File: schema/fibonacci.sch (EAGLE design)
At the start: 29 parts, among them IC1 DS1307, J1 POWER_JACK

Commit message: Board schema and layout v0.9
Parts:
- removed C6: 100nF, resistor:C-EU050-025X075
- removed U$1: RPI_SD_HOLDER, xose:RPI_SD_HOLDER
- added C3: 100nF, xose:C-EU050-025X075
- added U$2: MicroSD, xose:MICROSD-HRS_DM3D
- 16MHZ: value (none) -> 16MHz; device special:XTAL/S -> xose:XTAL/S
- BATT: device adafruit:CR2032SMT -> xose:CR2032SMT
- BUTTON1: value TACTILE_BUTTON -> B1
- BUTTON2: value TACTILE_BUTTON -> B2
- BUTTON3: value TACTILE_BUTTON -> B3
- BUTTON4: value TACTILE_BUTTON -> B4
- C1, C2, C4, C5: device rcl:C-EU025-025X050 -> xose:C-EU050-025X075
- CRYSTAL: device adafruit:CRYSTALTC38H -> xose:CRYSTAL_TC38H
- IC1: device adafruit:DS1307 -> xose:DS1307
- J1: value POWER_JACK -> POWER_JACKPTH; device SparkFun-Connectors:POWER_JACKPTH -> xose:POWER_JACKPTH
- LED_TERMINAL: value (none) -> M03-SCREW-2.5MM; device SparkFun-Connectors:M03-SCREW-5MM -> xose:M03-SCREW-2.5MM
- MUC: device SparkFun-DigitalIC:ATMEGA328P_PDIP -> xose:ATMEGA328P_PDIP
- POWER_TERMINAL: value (none) -> M02-SCREW-2.5MM; device SparkFun-Connectors:M025MM -> xose:M02-SCREW-2.5MM
- R1, R2, R3, R4, R5, R6, R7, R8: device SparkFun-Resistors:RESISTORPTH-1/4W -> xose:RESISTOR
- R9: value 10K -> 1K8; device SparkFun-Resistors:RESISTORPTH-1/4W -> xose:RESISTOR
- REGULATOR: value LP2950Z -> TSC295033; device national-semiconductor:LP2950Z -> xose:LP2950Z
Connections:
- new net N$14: U$2.GND1
- new net N$15: U$2.GND2
- new net N$16: U$2.GND3
- new net N$17: U$2.GND4
- net 3V3: now also U$2.3V3; no longer U$1.3V3
- net 5V: now also POWER_TERMINAL.1, R9.2; no longer POWER_TERMINAL.2, R9.1
- net DATA: now also MUC.PD4(XCK/T0); no longer MUC.PB1(OC1A)
- net DTR: now also C3.2; no longer C6.1
- net GND: now also C4.2, C5.2, POWER_TERMINAL.2, U$2.CMD, U$2.VSS; no longer C4.1, C5.1, POWER_TERMINAL.1, U$1.GND1, U$1.GND2
- net MISO: now also U$2.MISO; no longer U$1.MISO
- net N$1: now also C3.1, R9.1; no longer C6.2, R9.2
- net N$2: now also C4.1; no longer C4.2
- net N$3: now also C5.1; no longer C5.2
- net N$4: now also BATT.+; no longer BATT.+1
- net SD_MOSI: now also U$2.MOSI; no longer U$1.MOSI
- net SD_SCK: now also U$2.SCK; no longer U$1.SCK
- net SD_SS: now also U$2.SS; no longer U$1.SS
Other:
- moved on the sheet: BATT, C4, C5, POWER_TERMINAL

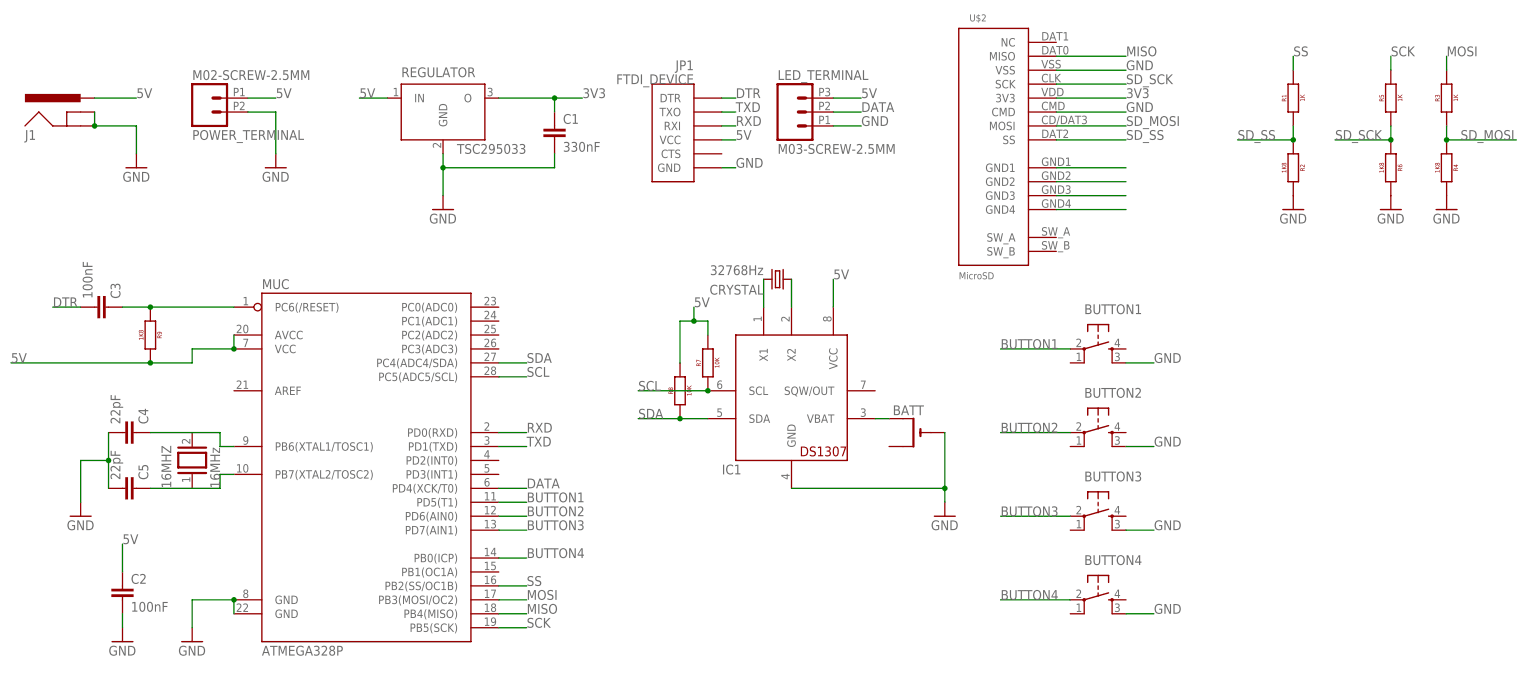
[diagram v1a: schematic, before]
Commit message: Added beefier terminals to board
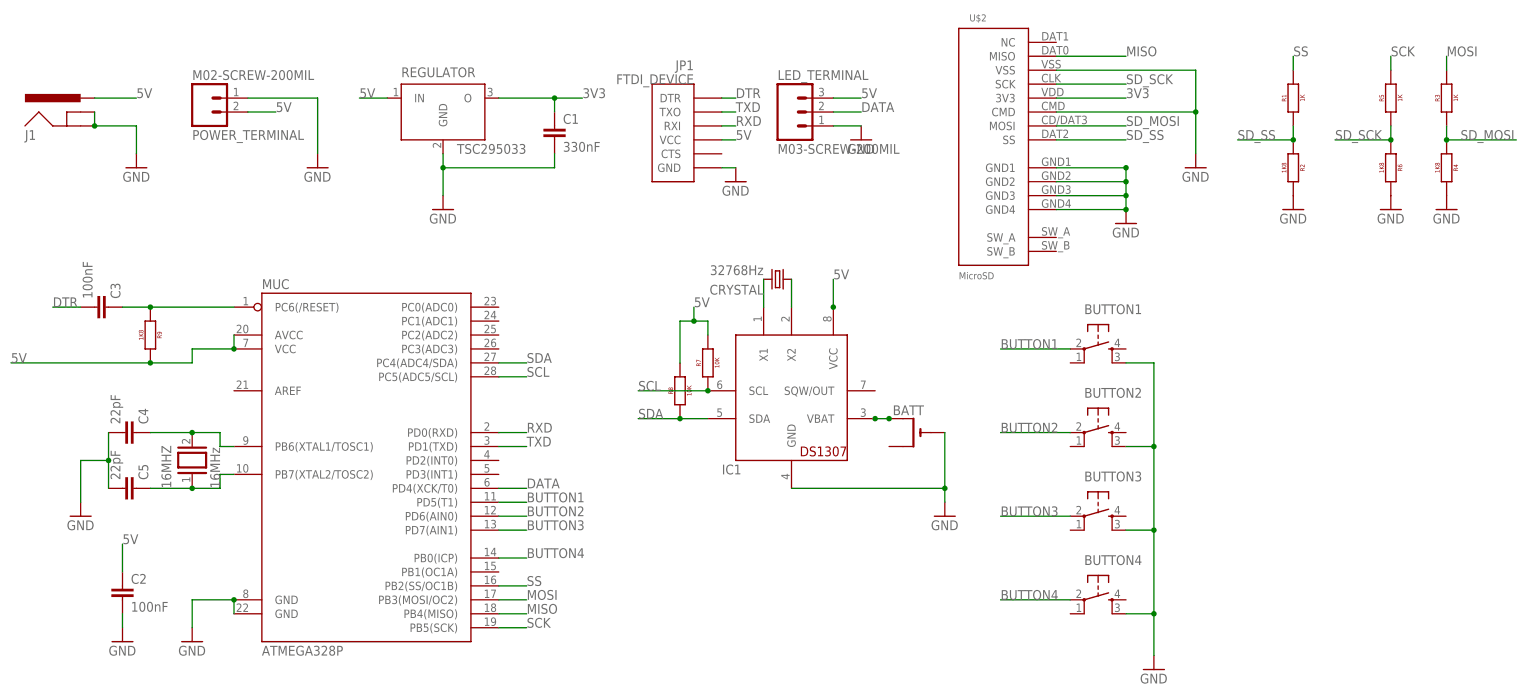
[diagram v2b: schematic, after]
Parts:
- LED_TERMINAL: value M03-SCREW-2.5MM -> M03-SCREW-200MIL; device xose:M03-SCREW-2.5MM -> xose:M03-SCREW-200MIL
- POWER_TERMINAL: value M02-SCREW-2.5MM -> M02-SCREW-200MIL; device xose:M02-SCREW-2.5MM -> xose:M02-SCREW-200MIL
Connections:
- removed net N$14: U$2.GND1
- removed net N$15: U$2.GND2
- removed net N$16: U$2.GND3
- removed net N$17: U$2.GND4
- net 5V: now also POWER_TERMINAL.2; no longer POWER_TERMINAL.1
- net GND: now also POWER_TERMINAL.1, U$2.GND1, U$2.GND2, U$2.GND3, U$2.GND4; no longer POWER_TERMINAL.2
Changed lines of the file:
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@@
 <part name="BUTTON3" library="xose" deviceset="TACTILE_BUTTON" device="" value="B3"/>
 <part name="BUTTON4" library="xose" deviceset="TACTILE_BUTTON" device="" value="B4"/>
-<part name="POWER_TERMINAL" library="xose" deviceset="M02-SCREW-2.5MM" device=""/>
-<part name="LED_TERMINAL" library="xose" deviceset="M03-SCREW-2.5MM" device=""/>
+<part name="POWER_TERMINAL" library="xose" deviceset="M02-SCREW-200MIL" device=""/>
+<part name="LED_TERMINAL" library="xose" deviceset="M03-SCREW-200MIL" device=""/>
 <part name="GND1" library="SparkFun-Aesthetics" deviceset="GND" device=""/>
 <part name="GND5" library="SparkFun-Aesthetics" deviceset="GND" device=""/>
@@
 <part name="R9" library="xose" deviceset="RESISTOR" device="" value="1K8"/>
 <part name="U$2" library="xose" deviceset="MICROSD-HRS_DM3D" device="" value="MicroSD"/>
+<part name="GND11" library="SparkFun-Aesthetics" deviceset="GND" device=""/>
+<part name="GND12" library="SparkFun-Aesthetics" deviceset="GND" device=""/>
+<part name="GND13" library="SparkFun-Aesthetics" deviceset="GND" device=""/>
+<part name="GND14" library="SparkFun-Aesthetics" deviceset="GND" device=""/>
+<part name="GND15" library="SparkFun-Aesthetics" deviceset="GND" device=""/>
 </parts>
 <sheets>
@@
 <instance part="POWER_TERMINAL" gate="G$1" x="-10.16" y="96.52" rot="MR180"/>
 <instance part="LED_TERMINAL" gate="G$1" x="96.52" y="96.52"/>
-<instance part="GND1" gate="1" x="2.54" y="86.36"/>
+<instance part="GND1" gate="1" x="10.16" y="86.36"/>
 <instance part="GND5" gate="1" x="124.46" y="22.86"/>
 <instance part="GND7" gate="1" x="33.02" y="78.74"/>
@@
 <instance part="R9" gate="G$1" x="-20.32" y="55.88" rot="R270"/>
 <instance part="U$2" gate="G$1" x="127" y="86.36"/>
+<instance part="GND11" gate="1" x="157.48" y="76.2"/>
+<instance part="GND12" gate="1" x="170.18" y="86.36"/>
+<instance part="GND13" gate="1" x="109.22" y="91.44"/>
+<instance part="GND14" gate="1" x="86.36" y="83.82"/>
+<instance part="GND15" gate="1" x="162.56" y="-5.08"/>
 </instances>
 <busses>
@@
 </segment>
 <segment>
-<pinref part="GND1" gate="1" pin="GND"/>
-<wire x1="2.54" y1="96.52" x2="2.54" y2="88.9" width="0.1524" layer="91"/>
-<pinref part="POWER_TERMINAL" gate="G$1" pin="2"/>
-<wire x1="2.54" y1="96.52" x2="-2.54" y2="96.52" width="0.1524" layer="91"/>
-</segment>
-<segment>
 <pinref part="LED_TERMINAL" gate="G$1" pin="1"/>
 <wire x1="104.14" y1="93.98" x2="109.22" y2="93.98" width="0.1524" layer="91"/>
-<label x="109.22" y="93.98" size="1.778" layer="95"/>
+<pinref part="GND13" gate="1" pin="GND"/>
 </segment>
 <segment>
@@
 <pinref part="BUTTON1" gate="G$1" pin="SWB2"/>
 <wire x1="157.48" y1="50.8" x2="162.56" y2="50.8" width="0.1524" layer="91"/>
-<label x="162.56" y="50.8" size="1.778" layer="95"/>
-</segment>
-<segment>
+<pinref part="GND15" gate="1" pin="GND"/>
+<wire x1="162.56" y1="50.8" x2="162.56" y2="35.56" width="0.1524" layer="91"/>
+<pinref part="BUTTON4" gate="G$1" pin="SWB2"/>
+<wire x1="162.56" y1="35.56" x2="162.56" y2="20.32" width="0.1524" layer="91"/>
+<wire x1="162.56" y1="20.32" x2="162.56" y2="5.08" width="0.1524" layer="91"/>
+<wire x1="162.56" y1="5.08" x2="162.56" y2="-2.54" width="0.1524" layer="91"/>
+<wire x1="157.48" y1="5.08" x2="162.56" y2="5.08" width="0.1524" layer="91"/>
+<junction x="162.56" y="5.08"/>
+<pinref part="BUTTON3" gate="G$1" pin="SWB2"/>
+<wire x1="157.48" y1="20.32" x2="162.56" y2="20.32" width="0.1524" layer="91"/>
+<junction x="162.56" y="20.32"/>
 <pinref part="BUTTON2" gate="G$1" pin="SWB2"/>
 <wire x1="157.48" y1="35.56" x2="162.56" y2="35.56" width="0.1524" layer="91"/>
-<label x="162.56" y="35.56" size="1.778" layer="95"/>
-</segment>
-<segment>
-<pinref part="BUTTON3" gate="G$1" pin="SWB2"/>
-<wire x1="157.48" y1="20.32" x2="162.56" y2="20.32" width="0.1524" layer="91"/>
-<label x="162.56" y="20.32" size="1.778" layer="95"/>
-</segment>
-<segment>
-<pinref part="BUTTON4" gate="G$1" pin="SWB2"/>
-<wire x1="157.48" y1="5.08" x2="162.56" y2="5.08" width="0.1524" layer="91"/>
-<label x="162.56" y="5.08" size="1.778" layer="95"/>
+<junction x="162.56" y="35.56"/>
 </segment>
 <segment>
 <pinref part="JP1" gate="G$1" pin="GND"/>
 <wire x1="83.82" y1="86.36" x2="86.36" y2="86.36" width="0.1524" layer="91"/>
-<label x="86.36" y="86.36" size="1.778" layer="95"/>
+<pinref part="GND14" gate="1" pin="GND"/>
 </segment>
 <segment>
 <pinref part="U$2" gate="G$1" pin="VSS"/>
-<wire x1="144.78" y1="104.14" x2="157.48" y2="104.14" width="0.1524" layer="91"/>
-<label x="157.48" y="104.14" size="1.778" layer="95"/>
-</segment>
-<segment>
-<wire x1="144.78" y1="96.52" x2="157.48" y2="96.52" width="0.1524" layer="91"/>
-<label x="157.48" y="96.52" size="1.778" layer="95"/>
+<wire x1="144.78" y1="104.14" x2="170.18" y2="104.14" width="0.1524" layer="91"/>
+<wire x1="170.18" y1="104.14" x2="170.18" y2="96.52" width="0.1524" layer="91"/>
 <pinref part="U$2" gate="G$1" pin="CMD"/>
+<wire x1="170.18" y1="96.52" x2="170.18" y2="88.9" width="0.1524" layer="91"/>
+<wire x1="144.78" y1="96.52" x2="170.18" y2="96.52" width="0.1524" layer="91"/>
+<pinref part="GND12" gate="1" pin="GND"/>
+<junction x="170.18" y="96.52"/>
+</segment>
+<segment>
+<pinref part="U$2" gate="G$1" pin="GND4"/>
+<wire x1="144.78" y1="78.74" x2="157.48" y2="78.74" width="0.1524" layer="91"/>
+<pinref part="GND11" gate="1" pin="GND"/>
+<pinref part="U$2" gate="G$1" pin="GND1"/>
+<wire x1="144.78" y1="86.36" x2="157.48" y2="86.36" width="0.1524" layer="91"/>
+<wire x1="157.48" y1="86.36" x2="157.48" y2="83.82" width="0.1524" layer="91"/>
+<pinref part="U$2" gate="G$1" pin="GND3"/>
+<wire x1="157.48" y1="83.82" x2="157.48" y2="81.28" width="0.1524" layer="91"/>
+<wire x1="157.48" y1="81.28" x2="157.48" y2="78.74" width="0.1524" layer="91"/>
+<wire x1="144.78" y1="81.28" x2="157.48" y2="81.28" width="0.1524" layer="91"/>
+<junction x="157.48" y="81.28"/>
+<pinref part="U$2" gate="G$1" pin="GND2"/>
+<wire x1="144.78" y1="83.82" x2="157.48" y2="83.82" width="0.1524" layer="91"/>
+<junction x="157.48" y="83.82"/>
+<junction x="157.48" y="78.74"/>
+<junction x="157.48" y="86.36"/>
+</segment>
+<segment>
+<pinref part="POWER_TERMINAL" gate="G$1" pin="1"/>
+<wire x1="-2.54" y1="99.06" x2="10.16" y2="99.06" width="0.1524" layer="91"/>
+<wire x1="10.16" y1="99.06" x2="10.16" y2="88.9" width="0.1524" layer="91"/>
+<pinref part="GND1" gate="1" pin="GND"/>
 </segment>
 </net>
@@
 <wire x1="104.14" y1="60.96" x2="104.14" y2="66.04" width="0.1524" layer="91"/>
 <label x="104.14" y="66.04" size="1.778" layer="95"/>
+<junction x="104.14" y="60.96"/>
 </segment>
 <segment>
@@
 </segment>
 <segment>
-<pinref part="POWER_TERMINAL" gate="G$1" pin="1"/>
-<wire x1="-2.54" y1="99.06" x2="2.54" y2="99.06" width="0.1524" layer="91"/>
-<label x="2.54" y="99.06" size="1.778" layer="95"/>
+<pinref part="POWER_TERMINAL" gate="G$1" pin="2"/>
+<wire x1="-2.54" y1="96.52" x2="2.54" y2="96.52" width="0.1524" layer="91"/>
+<label x="2.54" y="96.52" size="1.778" layer="95"/>
 </segment>
 </net>
@@
 <pinref part="C4" gate="G$1" pin="1"/>
 <wire x1="-12.7" y1="38.1" x2="-20.32" y2="38.1" width="0.1524" layer="91"/>
+<junction x="-12.7" y="38.1"/>
 </segment>
 </net>
@@
 <pinref part="C5" gate="G$1" pin="1"/>
 <wire x1="-12.7" y1="27.94" x2="-20.32" y2="27.94" width="0.1524" layer="91"/>
+<junction x="-12.7" y="27.94"/>
 </segment>
 </net>
@@
 </segment>
 </net>
-<net name="N$14" class="0">
-<segment>
-<pinref part="U$2" gate="G$1" pin="GND1"/>
-<wire x1="144.78" y1="86.36" x2="157.48" y2="86.36" width="0.1524" layer="91"/>
-</segment>
-</net>
-<net name="N$15" class="0">
-<segment>
-<pinref part="U$2" gate="G$1" pin="GND2"/>
-<wire x1="144.78" y1="83.82" x2="157.48" y2="83.82" width="0.1524" layer="91"/>
-</segment>
-</net>
-<net name="N$16" class="0">
-<segment>
-<pinref part="U$2" gate="G$1" pin="GND3"/>
-<wire x1="144.78" y1="81.28" x2="157.48" y2="81.28" width="0.1524" layer="91"/>
-</segment>
-</net>
-<net name="N$17" class="0">
-<segment>
-<pinref part="U$2" gate="G$1" pin="GND4"/>
-<wire x1="144.78" y1="78.74" x2="157.48" y2="78.74" width="0.1524" layer="91"/>
-</segment>
-</net>
 <net name="N$4" class="0">
 <segment>
@@
 <pinref part="BATT" gate="G$1" pin="+"/>
 <wire x1="111.76" y1="40.64" x2="114.3" y2="40.64" width="0.1524" layer="91"/>
-</segment>
-</net>
+<junction x="114.3" y="40.64"/>
+<junction x="111.76" y="40.64"/>
+</segment>
+</net>

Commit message: Final PCB version and gerbers
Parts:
- removed MUC: ATMEGA328P, xose:ATMEGA328P_PDIP
- added IC2: DS1307, xose:DS1307
- IC1: value DS1307 -> ATMEGA328P; device xose:DS1307 -> xose:ATMEGA328P_PDIP
- U$2: value MicroSD -> uSD
- renumbered 16MHZ to XTAL1, CRYSTAL to XTAL2, REGULATOR to LDO1
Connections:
- net 5V: now also IC1.AVCC, IC2.VCC; no longer MUC.AVCC, MUC.VCC
- net BUTTON1: now also IC1.PD5(T1); no longer MUC.PD5(T1)
- net BUTTON2: now also IC1.PD6(AIN0); no longer MUC.PD6(AIN0)
- net BUTTON3: now also IC1.PD7(AIN1); no longer MUC.PD7(AIN1)
- net BUTTON4: now also IC1.PB0(ICP); no longer MUC.PB0(ICP)
- net DATA: now also IC1.PD4(XCK/T0); no longer MUC.PD4(XCK/T0)
- net GND: now also IC1.GND@1, IC1.GND@2, IC2.GND; no longer IC1.GND, MUC.GND@1, MUC.GND@2
- net MISO: now also IC1.PB4(MISO); no longer MUC.PB4(MISO)
- net MOSI: now also IC1.PB3(MOSI/OC2); no longer MUC.PB3(MOSI/OC2)
- net N$1: now also IC1.PC6(/RESET); no longer MUC.PC6(/RESET)
- net N$2: now also IC1.PB6(XTAL1/TOSC1); no longer MUC.PB6(XTAL1/TOSC1)
- net N$3: now also IC1.PB7(XTAL2/TOSC2); no longer MUC.PB7(XTAL2/TOSC2)
- net N$4: now also IC2.VBAT; no longer IC1.VBAT
- net N$5: now also IC2.X1; no longer IC1.X1
- net N$6: now also IC2.X2; no longer IC1.X2
- net RXD: now also IC1.PD0(RXD); no longer MUC.PD0(RXD)
- net SCK: now also IC1.PB5(SCK); no longer MUC.PB5(SCK)
- net SCL: now also IC1.PC5(ADC5/SCL), IC2.SCL; no longer IC1.SCL, MUC.PC5(ADC5/SCL)
- net SDA: now also IC1.PC4(ADC4/SDA), IC2.SDA; no longer IC1.SDA, MUC.PC4(ADC4/SDA)
- net SS: now also IC1.PB2(SS/OC1B); no longer MUC.PB2(SS/OC1B)
- net TXD: now also IC1.PD1(TXD); no longer MUC.PD1(TXD)

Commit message: Schema and board layout, datasheets
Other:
- moved on the sheet: LDO1

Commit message: Version 1.2 of the layout sent to fab
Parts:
- R1, R2, R3, R4, R5, R6, R7, R8, R9: device xose:RESISTOR -> xose:RESISTOR-400MIL
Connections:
- net GND: no longer U$2.CMD
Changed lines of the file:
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@@
 <part name="IC2" library="xose" deviceset="DS1307" device=""/>
 <part name="XTAL2" library="xose" deviceset="CRYSTAL_TC38H" device="" value="32768Hz"/>
-<part name="R1" library="xose" deviceset="RESISTOR" device="" value="1K"/>
-<part name="R3" library="xose" deviceset="RESISTOR" device="" value="1K"/>
-<part name="R5" library="xose" deviceset="RESISTOR" device="" value="1K"/>
-<part name="R2" library="xose" deviceset="RESISTOR" device="" value="1K8"/>
-<part name="R4" library="xose" deviceset="RESISTOR" device="" value="1K8"/>
-<part name="R6" library="xose" deviceset="RESISTOR" device="" value="1K8"/>
-<part name="R7" library="xose" deviceset="RESISTOR" device="" value="10K"/>
-<part name="R8" library="xose" deviceset="RESISTOR" device="" value="10K"/>
+<part name="R1" library="xose" deviceset="RESISTOR-400MIL" device="" value="1K"/>
+<part name="R3" library="xose" deviceset="RESISTOR-400MIL" device="" value="1K"/>
+<part name="R5" library="xose" deviceset="RESISTOR-400MIL" device="" value="1K"/>
+<part name="R2" library="xose" deviceset="RESISTOR-400MIL" device="" value="1K8"/>
+<part name="R4" library="xose" deviceset="RESISTOR-400MIL" device="" value="1K8"/>
+<part name="R6" library="xose" deviceset="RESISTOR-400MIL" device="" value="1K8"/>
+<part name="R7" library="xose" deviceset="RESISTOR-400MIL" device="" value="10K"/>
+<part name="R8" library="xose" deviceset="RESISTOR-400MIL" device="" value="10K"/>
 <part name="BUTTON1" library="xose" deviceset="TACTILE_BUTTON" device="" value="B1"/>
 <part name="BUTTON2" library="xose" deviceset="TACTILE_BUTTON" device="" value="B2"/>
@@
 <part name="GND10" library="SparkFun-Aesthetics" deviceset="GND" device=""/>
 <part name="JP1" library="SparkFun-Connectors" deviceset="FTDI_DEVICE" device=""/>
-<part name="R9" library="xose" deviceset="RESISTOR" device="" value="1K8"/>
+<part name="R9" library="xose" deviceset="RESISTOR-400MIL" device="" value="1K8"/>
 <part name="U$2" library="xose" deviceset="MICROSD-HRS_DM3D" device="" value="uSD"/>
 <part name="GND11" library="SparkFun-Aesthetics" deviceset="GND" device=""/>
@@
 <instance part="U$2" gate="G$1" x="127" y="86.36"/>
 <instance part="GND11" gate="1" x="157.48" y="76.2"/>
-<instance part="GND12" gate="1" x="170.18" y="86.36"/>
+<instance part="GND12" gate="1" x="172.72" y="99.06"/>
 <instance part="GND13" gate="1" x="109.22" y="91.44"/>
 <instance part="GND14" gate="1" x="86.36" y="83.82"/>
@@
 <segment>
 <pinref part="U$2" gate="G$1" pin="VSS"/>
-<wire x1="144.78" y1="104.14" x2="170.18" y2="104.14" width="0.1524" layer="91"/>
-<wire x1="170.18" y1="104.14" x2="170.18" y2="96.52" width="0.1524" layer="91"/>
-<pinref part="U$2" gate="G$1" pin="CMD"/>
-<wire x1="170.18" y1="96.52" x2="170.18" y2="88.9" width="0.1524" layer="91"/>
-<wire x1="144.78" y1="96.52" x2="170.18" y2="96.52" width="0.1524" layer="91"/>
+<wire x1="144.78" y1="104.14" x2="172.72" y2="104.14" width="0.1524" layer="91"/>
+<wire x1="172.72" y1="104.14" x2="172.72" y2="101.6" width="0.1524" layer="91"/>
 <pinref part="GND12" gate="1" pin="GND"/>
-<junction x="170.18" y="96.52"/>
-</segment>
-<segment>
+</segment>
+<segment>
